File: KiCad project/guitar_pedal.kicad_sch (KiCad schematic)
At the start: 39 parts, among them J1 NMJ6HCD2, J2 NMJ6HCD2, J3 AVR-ISP-6, SW1 SW_SPST, SW2 SWITCH_3PDT, U1 ATmega1284-P, U2 L7805, U3 TL061, U4 TL061, Y1 Crystal 16MHz

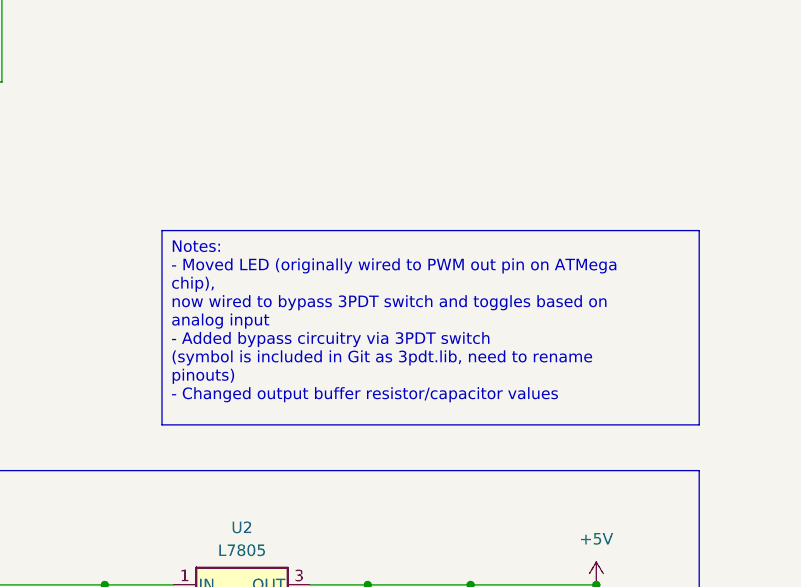
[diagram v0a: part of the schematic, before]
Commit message: Reorganized files. Added initial PCB. Added KiCad components. Some footprints added to schematic.
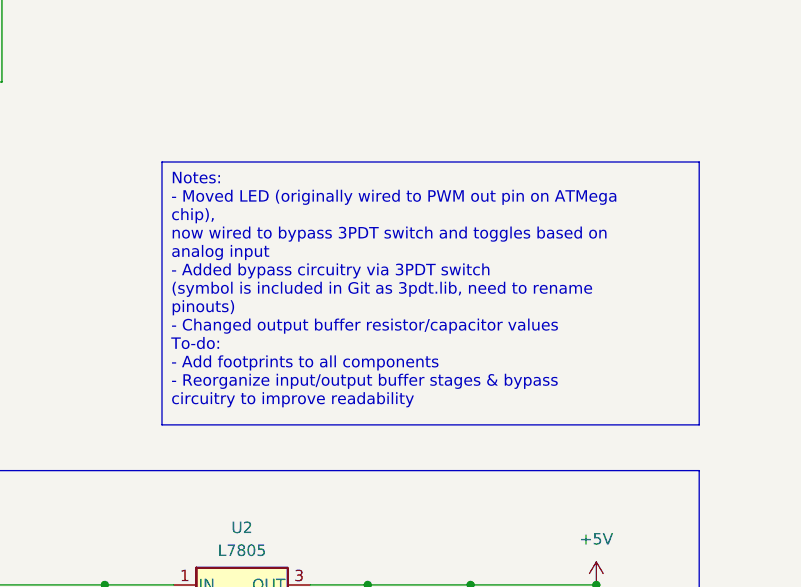
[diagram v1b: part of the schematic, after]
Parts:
- D1: footprint (none) -> LED_THT:LED_D3.0mm
- J3: footprint (none) -> User:AVR-ISP-6

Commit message: Added somes caps and resistors
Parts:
- added C15, C16, C17: 0.1uf, symbol Device:C_Small
- added R12: 10K, symbol Device:R_Small_US
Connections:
- net +5V: now also C16.2, C17.1, R12.1
- net GND: now also C15.2, C16.1, C17.2
- net at J3.5 (~{RST}), U1.9 (~{RESET}): now also R12.2
- net at U1.32 (AREF): now also C15.1
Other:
- moved on the sheet: RV1

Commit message: Changed some incorrect voltages.
Still needs to consolidate 2 individual op amps into the TL972IDR, dual op amp.
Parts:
- D2: value LED -> GREEN LED
- R11: value 220 -> 120
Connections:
- net +2V5 is gone; now on net +5V: R6.1
- net +5V: now also R11.1
- net +9V: no longer R11.1
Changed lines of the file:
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@@
-    (stroke (width 0) (type default))
-  )
-  (wire (pts (xy 231.14 57.15) (xy 231.14 59.69))
     (stroke (width 0) (type default))
   )
@@
   )
   (wire (pts (xy 161.29 140.97) (xy 171.45 140.97))
+    (stroke (width 0) (type default))
+  )
+  (wire (pts (xy 231.14 55.88) (xy 231.14 59.69))
     (stroke (width 0) (type default))
   )
@@
     )
   )
+  (symbol (lib_id "power:+5V") (at 265.43 71.12 0) (unit 1)
+    (in_bom yes) (on_board yes) (dnp no) (fields_autoplaced)
+    (property "Reference" "#PWR016" (at 265.43 74.93 0)
+      (effects (font (size 1.27 1.27)) hide)
+    )
+    (property "Value" "+5V" (at 265.43 66.04 0)
+      (effects (font (size 1.27 1.27)))
+    )
+    (property "Footprint" "" (at 265.43 71.12 0)
+      (effects (font (size 1.27 1.27)) hide)
+    )
+    (property "Datasheet" "" (at 265.43 71.12 0)
+      (effects (font (size 1.27 1.27)) hide)
+    )
+    (pin "1")
+    (instances
+      (project "guitar_pedal"
+        (path "/23db8aec-b53f-46f3-9e89-875dd8c49681"
+          (reference "#PWR016") (unit 1)
+        )
+      )
+    )
+  )
   (symbol (lib_id "power:GND") (at 191.77 99.06 0) (unit 1)
     (in_bom yes) (on_board yes) (dnp no) (fields_autoplaced)
@@
         (path "/23db8aec-b53f-46f3-9e89-875dd8c49681"
           (reference "C2") (unit 1)
-        )
-      )
-    )
-  )
-  (symbol (lib_id "power:+2V5") (at 265.43 71.12 0) (unit 1)
-    (in_bom yes) (on_board yes) (dnp no) (fields_autoplaced)
-    (property "Reference" "#PWR016" (at 265.43 74.93 0)
-      (effects (font (size 1.27 1.27)) hide)
-    )
-    (property "Value" "+2V5" (at 265.43 66.04 0)
-      (effects (font (size 1.27 1.27)))
-    )
-    (property "Footprint" "" (at 265.43 71.12 0)
-      (effects (font (size 1.27 1.27)) hide)
-    )
-    (property "Datasheet" "" (at 265.43 71.12 0)
-      (effects (font (size 1.27 1.27)) hide)
-    )
-    (pin "1")
-    (instances
-      (project "guitar_pedal"
-        (path "/23db8aec-b53f-46f3-9e89-875dd8c49681"
-          (reference "#PWR016") (unit 1)
         )
       )
@@
     )
   )
+  (symbol (lib_id "power:+5V") (at 231.14 55.88 0) (unit 1)
+    (in_bom yes) (on_board yes) (dnp no) (fields_autoplaced)
+    (property "Reference" "#PWR026" (at 231.14 59.69 0)
+      (effects (font (size 1.27 1.27)) hide)
+    )
+    (property "Value" "+5V" (at 231.14 50.8 0)
+      (effects (font (size 1.27 1.27)))
+    )
+    (property "Footprint" "" (at 231.14 55.88 0)
+      (effects (font (size 1.27 1.27)) hide)
+    )
+    (property "Datasheet" "" (at 231.14 55.88 0)
+      (effects (font (size 1.27 1.27)) hide)
+    )
+    (pin "1")
+    (instances
+      (project "guitar_pedal"
+        (path "/23db8aec-b53f-46f3-9e89-875dd8c49681"
+          (reference "#PWR026") (unit 1)
+        )
+      )
+    )
+  )
   (symbol (lib_id "power:+5V") (at 49.53 67.31 0) (unit 1)
     (in_bom yes) (on_board yes) (dnp no) (fields_autoplaced)
@@
   )
   (symbol (lib_id "Device:LED") (at 231.14 73.66 90) (unit 1)
-    (in_bom yes) (on_board yes) (dnp no) (fields_autoplaced)
+    (in_bom yes) (on_board yes) (dnp no)
     (property "Reference" "D2" (at 234.95 73.9775 90)
       (effects (font (size 1.27 1.27)) (justify right))
     )
-    (property "Value" "LED" (at 234.95 76.5175 90)
+    (property "Value" "GREEN LED" (at 234.95 76.5175 90)
       (effects (font (size 1.27 1.27)) (justify right))
     )
@@
     )
   )
-  (symbol (lib_id "power:+9V") (at 231.14 57.15 0) (unit 1)
-    (in_bom yes) (on_board yes) (dnp no) (fields_autoplaced)
-    (property "Reference" "#PWR026" (at 231.14 60.96 0)
-      (effects (font (size 1.27 1.27)) hide)
-    )
-    (property "Value" "+9V" (at 231.14 52.07 0)
-      (effects (font (size 1.27 1.27)))
-    )
-    (property "Footprint" "" (at 231.14 57.15 0)
-      (effects (font (size 1.27 1.27)) hide)
-    )
-    (property "Datasheet" "" (at 231.14 57.15 0)
-      (effects (font (size 1.27 1.27)) hide)
-    )
-    (pin "1")
-    (instances
-      (project "guitar_pedal"
-        (path "/23db8aec-b53f-46f3-9e89-875dd8c49681"
-          (reference "#PWR026") (unit 1)
-        )
-      )
-    )
-  )
   (symbol (lib_id "power:GND") (at 27.94 85.09 0) (unit 1)
     (in_bom yes) (on_board yes) (dnp no) (fields_autoplaced)
@@
       (effects (font (size 1.27 1.27)))
     )
-    (property "Value" "220" (at 231.14 63.5 90)
-      (effects (font (size 1.27 1.27)))
-    )
+    (property "Value" "120" (at 231.14 63.5 90)
+      (effects (font (size 1.27 1.27)))
+    )

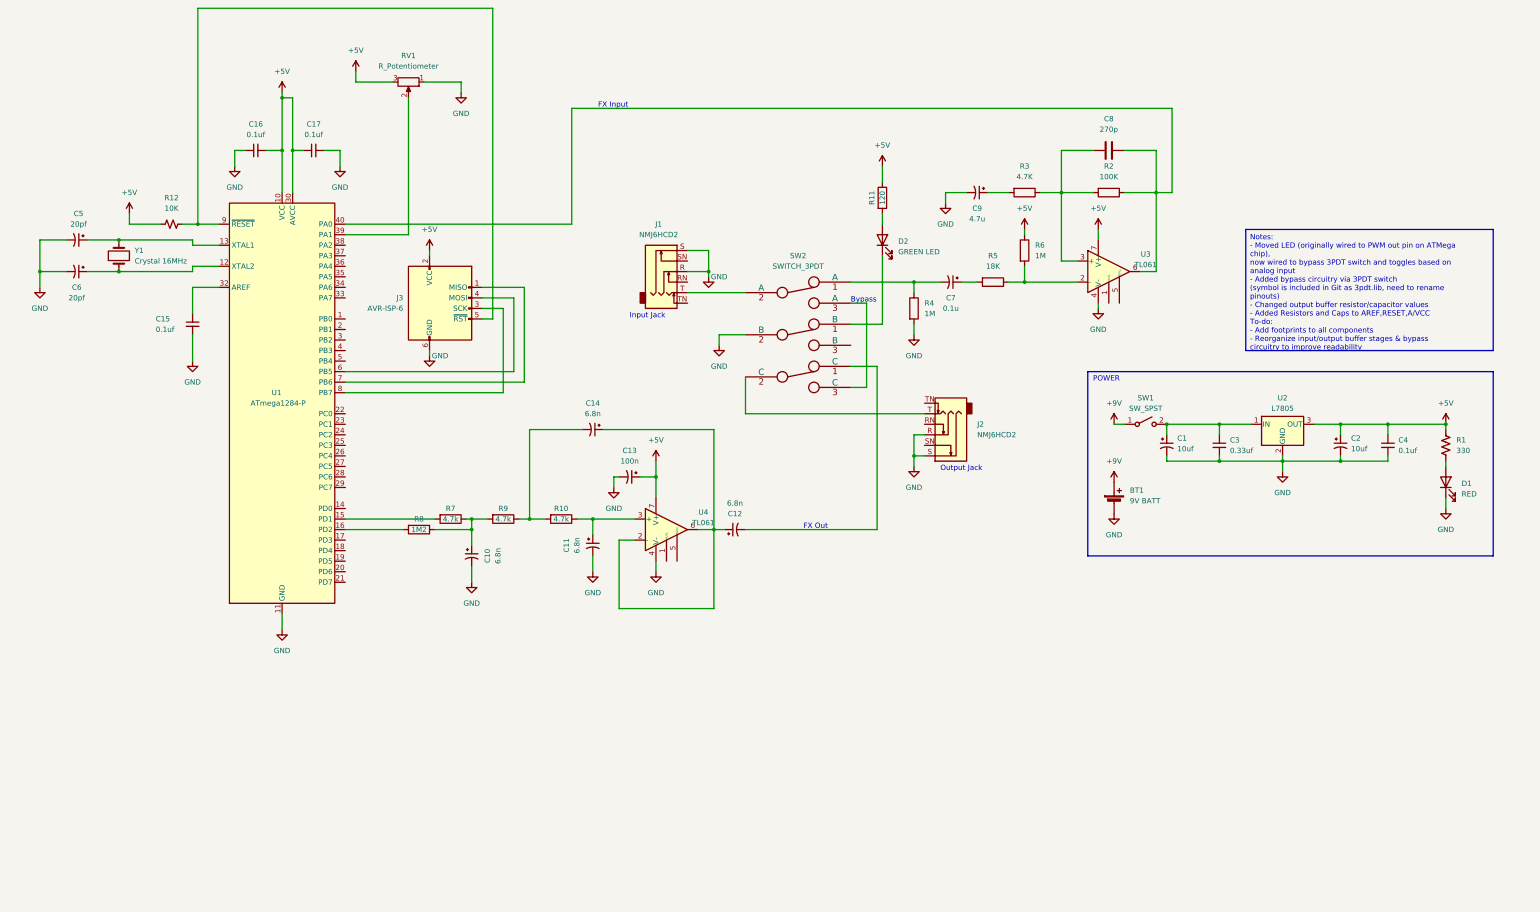
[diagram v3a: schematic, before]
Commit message: Overall schematic layout updated. Minor changes to components.
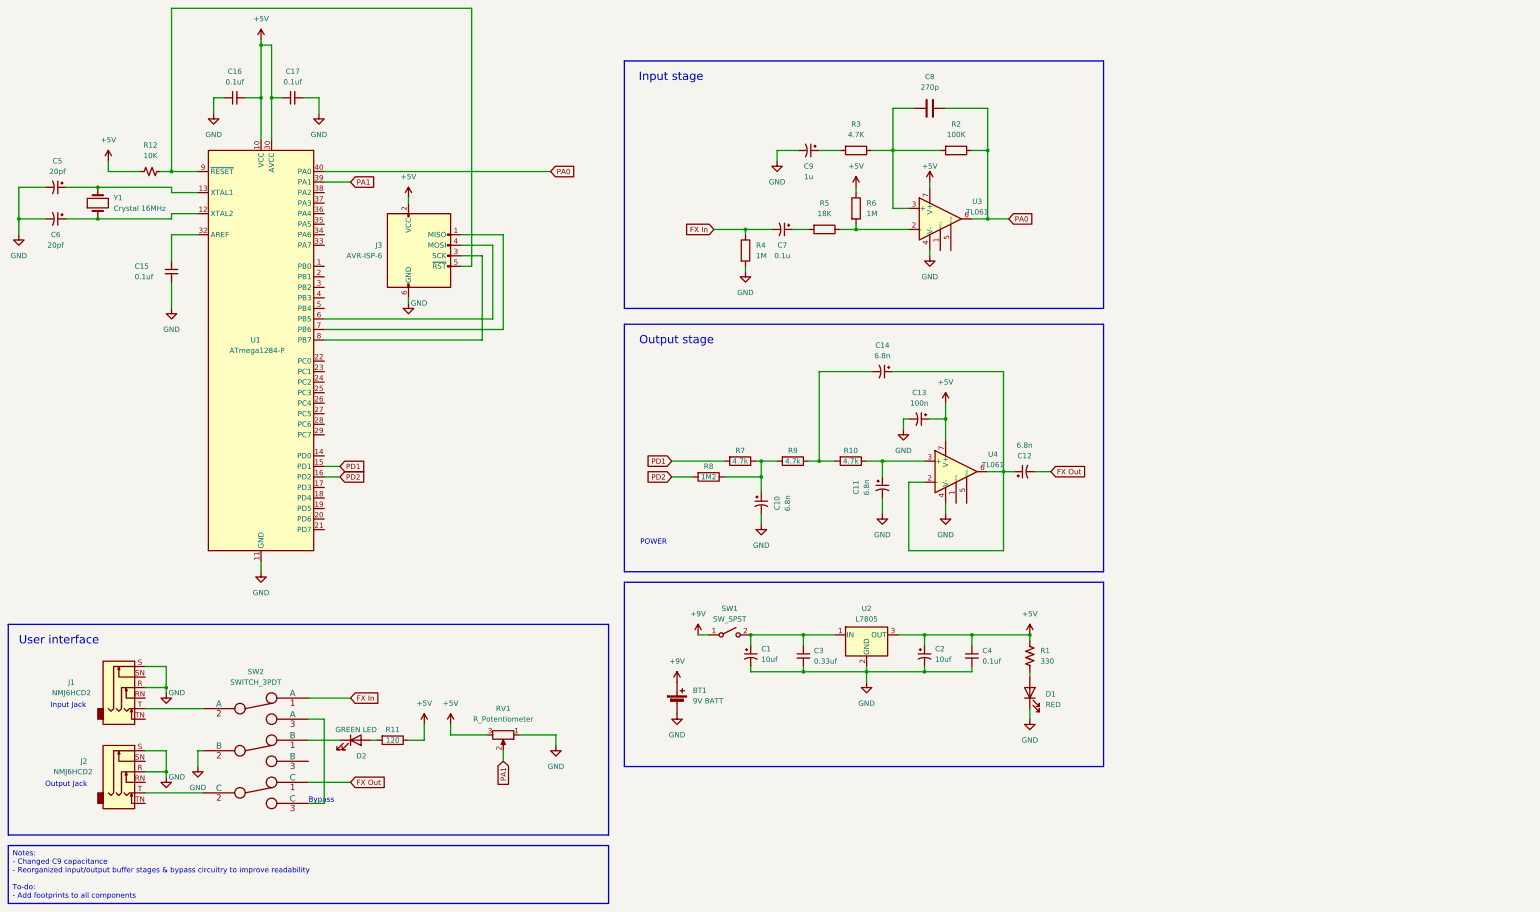
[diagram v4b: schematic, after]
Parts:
- C9: value 4.7u -> 1u
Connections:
- net FX In: now reaches C7.2, R4.1, SW2.1 (C)
- net PA1: now reaches RV1.2, U1.39 (PA1)
- net PD2: now reaches R8.2, U1.16 (PD2)
- net FX Out: now reaches C12.2, SW2.1 (C)
- net PA0: now reaches C8.2, R2.1, U1.40 (PA0), U3.6
- net PD1: now reaches R7.2, U1.15 (PD1)
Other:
- note added: "Input stage"
- note added: "Output stage"
- note added: "User interface"
- note removed: "FX Input"
- note removed: "FX Out"
- moved on the sheet: BT1, C1, C10, C11, C12, C13, C14, C15, C16, C17, C2, C3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

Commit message: Updated components with footprints, added to PCB
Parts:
- C1, C2: value 10uf -> 10u; footprint (none) -> Capacitor_SMD:CP_Elec_4x5.4
- C10, C11, C12, C13, C14, C7, C8: footprint (none) -> Capacitor_SMD:C_1206_3216Metric
- C15, C16, C17, C4: value 0.1uf -> 0.1u; footprint (none) -> Capacitor_SMD:C_1206_3216Metric
- C3: value 0.33uf -> 0.33u; footprint (none) -> Capacitor_SMD:C_1206_3216Metric
- C5, C6: value 20pf -> 22p; footprint (none) -> Capacitor_SMD:C_1206_3216Metric
- C9: footprint (none) -> Capacitor_SMD:C_Elec_4x5.4
- D1: footprint LED_THT:LED_D3.0mm -> LED_SMD:LED_0603_1608Metric
- D2: footprint (none) -> LED_THT:LED_D3.0mm
- R1, R10, R11, R12, R2, R3, R4, R5, R6, R7, R8, R9: footprint (none) -> Resistor_SMD:R_1206_3216Metric
- SW2: footprint (none) -> User:3PDT
- U1: footprint Package_DIP:DIP-40_W15.24mm -> Package_QFP:TQFP-44_10x10mm_P0.8mm
- U3: footprint (none) -> Package_SO:SOIC-8-1EP_3.9x4.9mm_P1.27mm_EP2.29x3mm
- Y1: footprint (none) -> Crystal:Crystal_HC49-U_Vertical

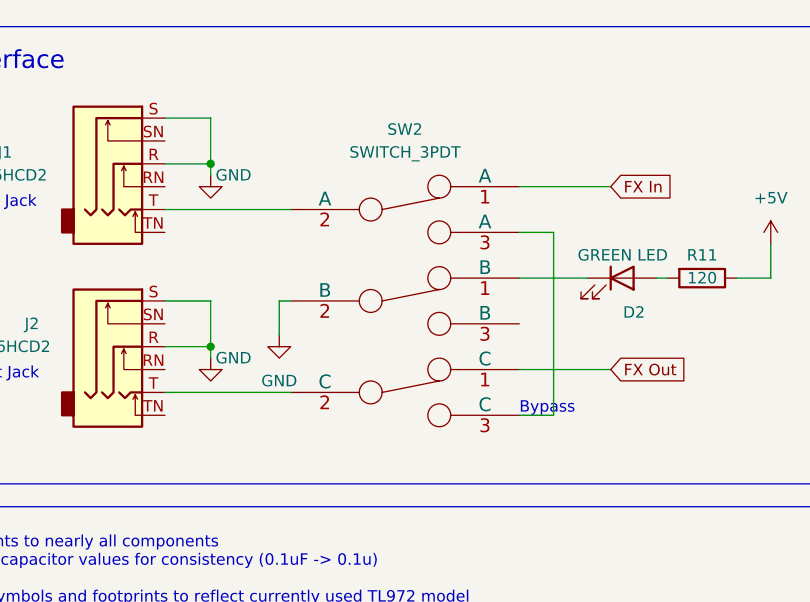
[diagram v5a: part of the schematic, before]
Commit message: Added traces to power supply and AVR modules in PCB.
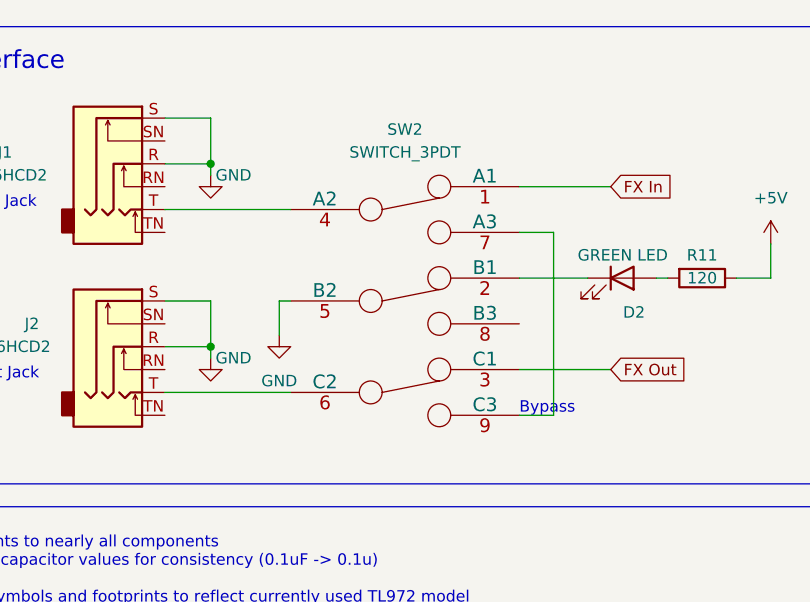
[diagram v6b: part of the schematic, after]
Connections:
- net FX Out: now also SW2.3 (C1); no longer SW2.1 (C)
- net GND: now also SW2.5 (B2); no longer SW2.2 (C)
- net at D2.1 (K): now also SW2.2 (B1); no longer SW2.1 (C)
- net at J2.T: now also SW2.6 (C2); no longer SW2.2 (C)
- net at J1.T: now also SW2.4 (A2); no longer SW2.2 (C)
- new net: SW2.7 (A3), SW2.9 (C3)
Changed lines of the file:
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@@
     )
     (pin "1")
-    (pin "1")
-    (pin "1")
-    (pin "2")
-    (pin "2")
     (pin "2")
     (pin "3")
-    (pin "3")
-    (pin "3")
+    (pin "4")
+    (pin "5")
+    (pin "6")
+    (pin "7")
+    (pin "8")
+    (pin "9")
     (instances
       (project "guitar_pedal"
